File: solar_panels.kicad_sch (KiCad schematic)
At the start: 72 parts, among them U15 MAX40200AUK, U4 BQ25570RGRR, U5 BQ25570RGRR, U6 MAX40200AUK

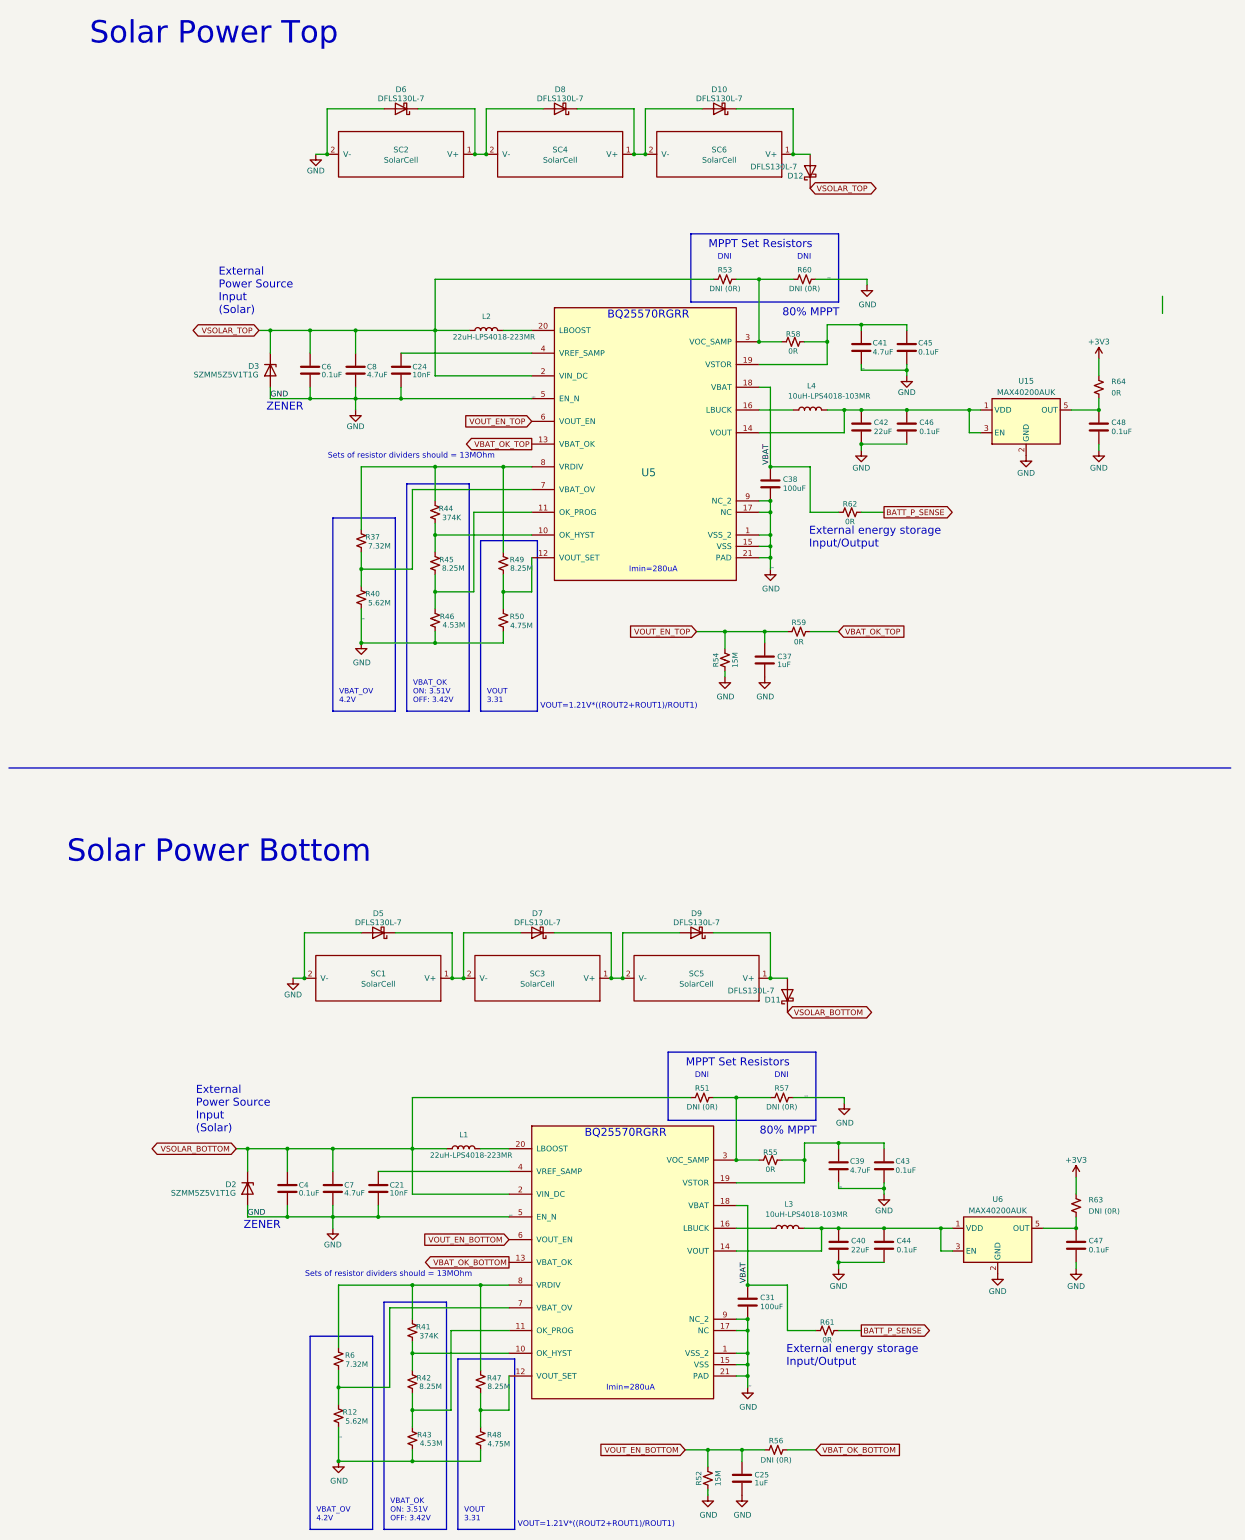
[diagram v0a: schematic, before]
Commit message: Fix ERC warnings
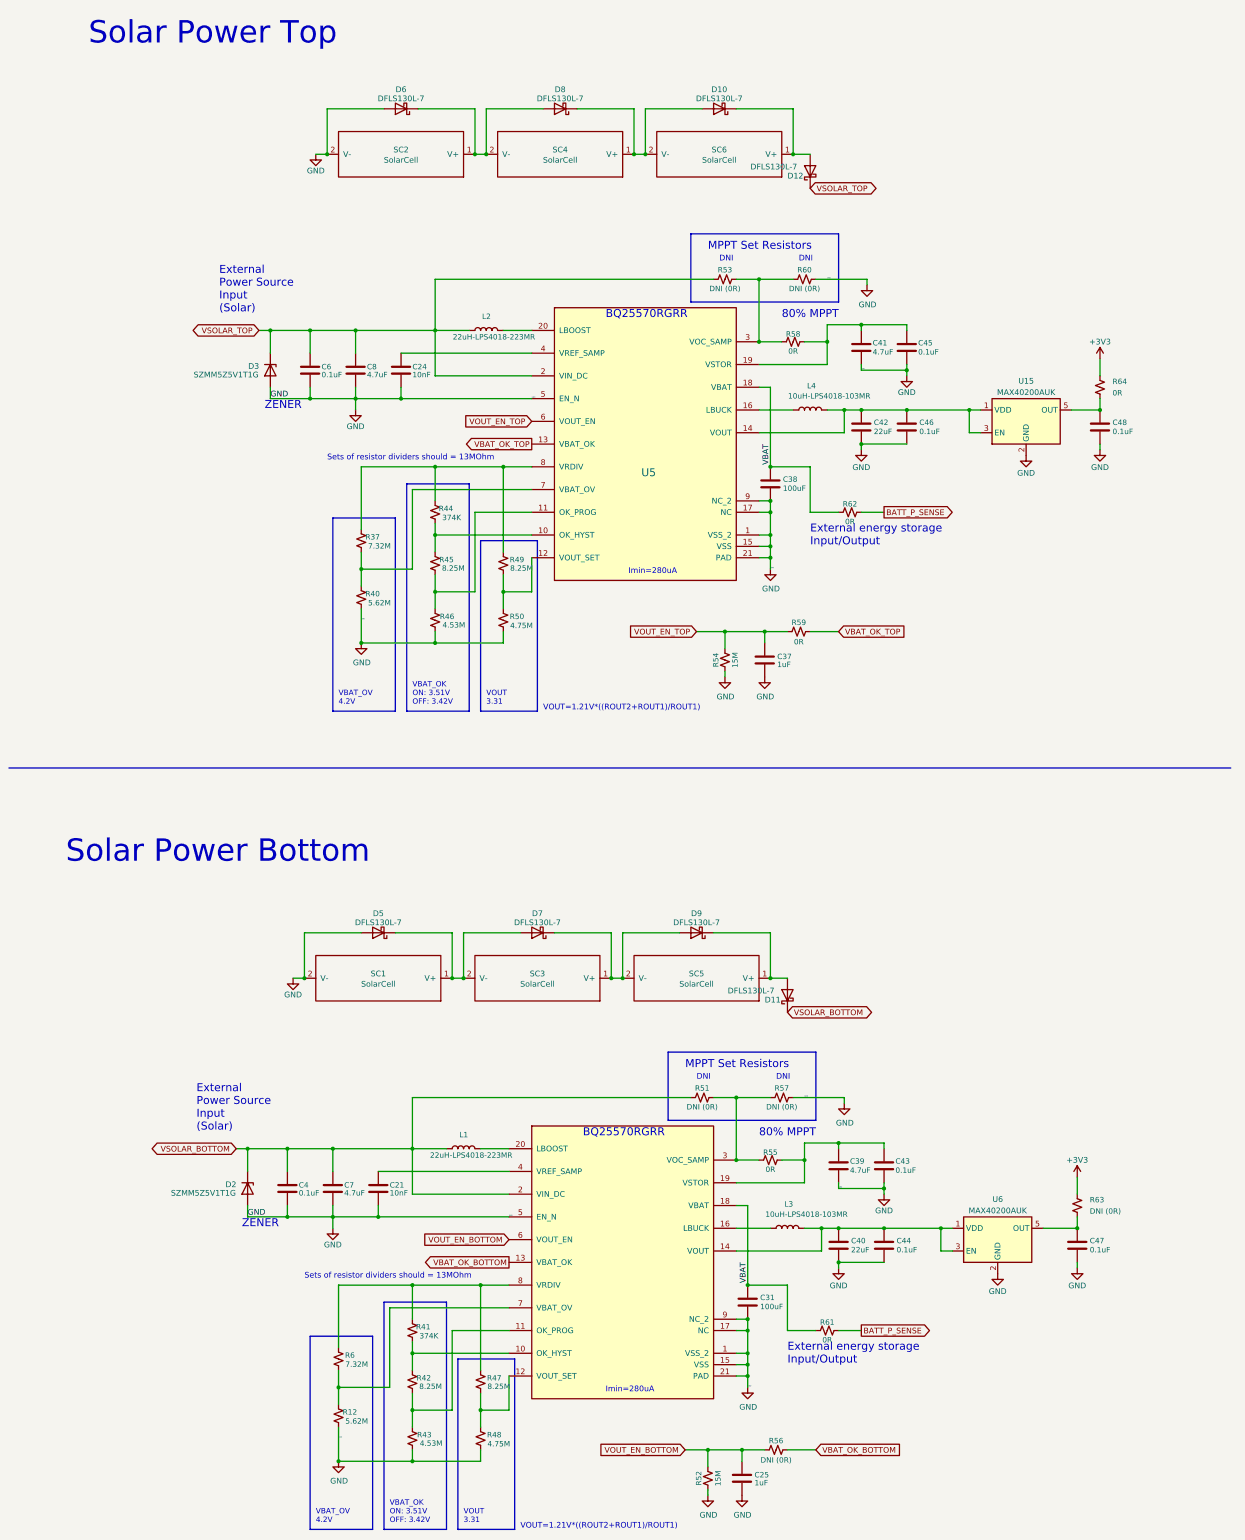
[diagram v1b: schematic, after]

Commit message: Reannotate schematic
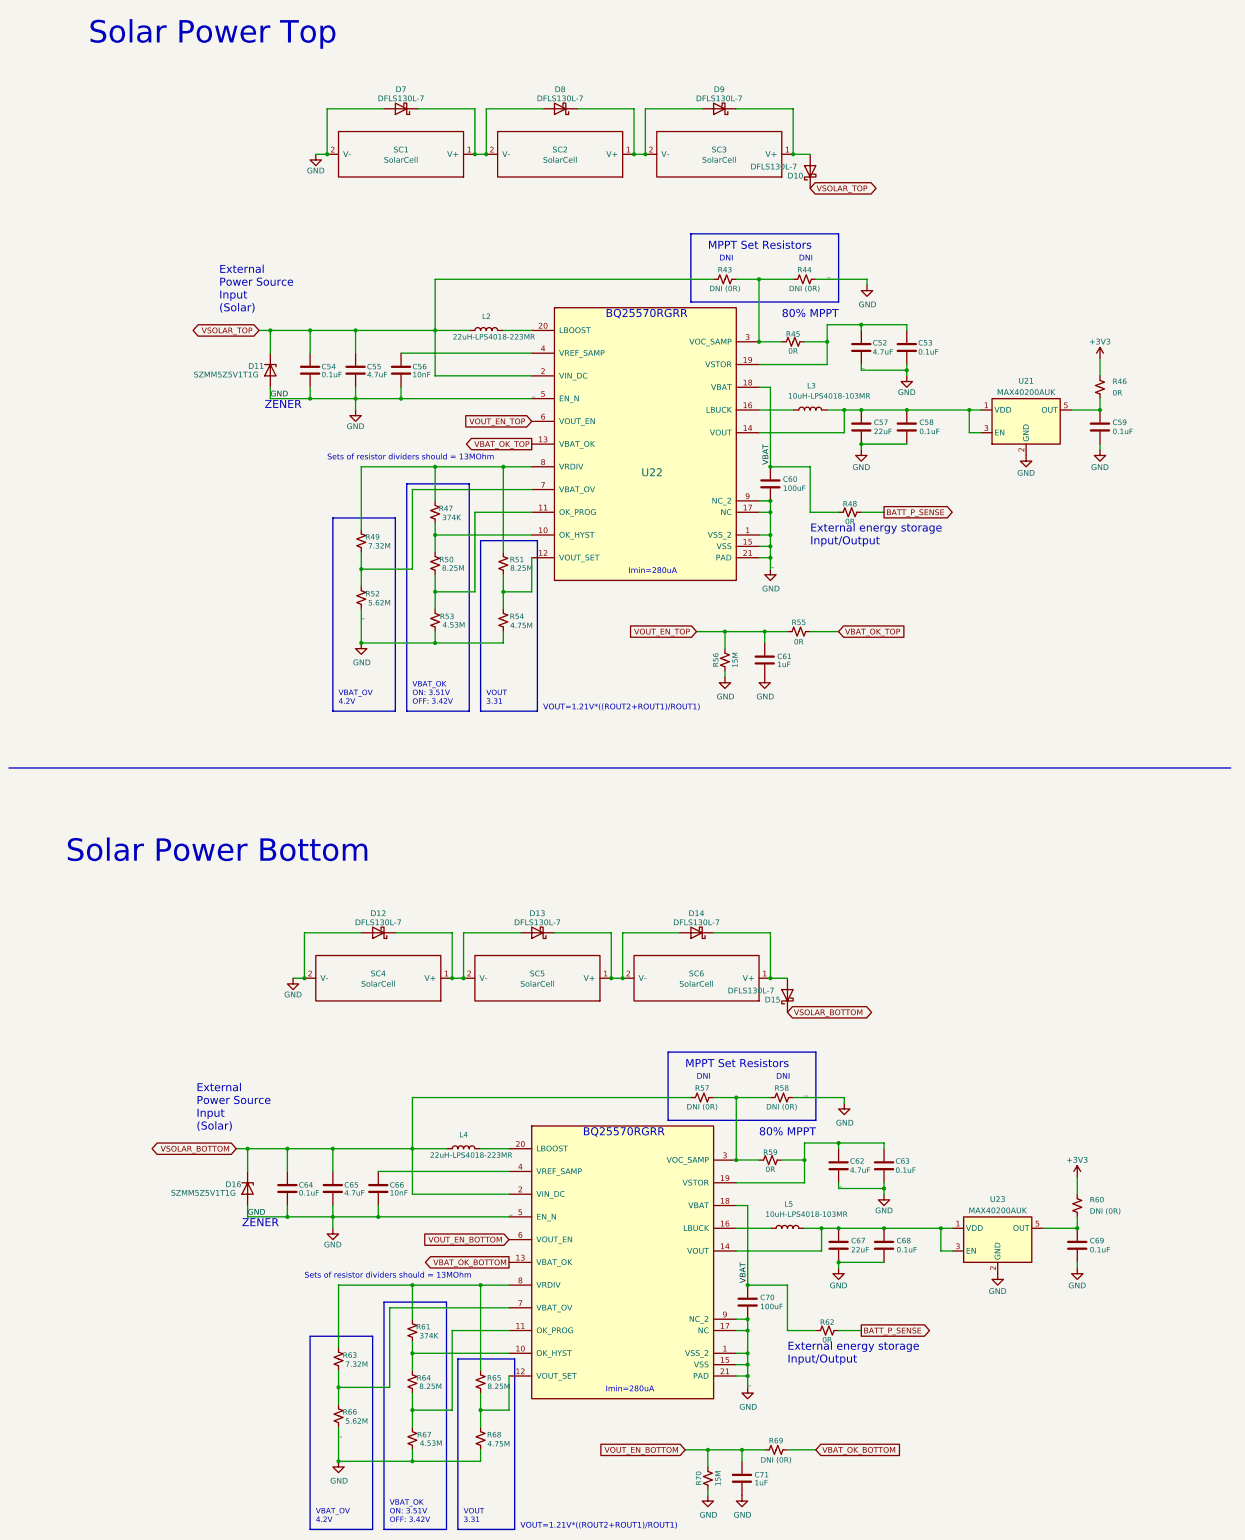
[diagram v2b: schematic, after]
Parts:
- renumbered C41 to C52, C45 to C53, C6 to C54, C8 to C55, C24 to C56, C42 to C57, C46 to C58, C48 to C59, C38 to C60, C37 to C61, C39 to C62, C43 to C63, C4 to C64, C7 to C65, C21 to C66, C40 to C67, C44 to C68, C47 to C69, C31 to C70, C25 to C71, D12 to D10, D3 to D11, D5 to D12, D7 to D13, D9 to D14, D11 to D15, D2 to D16, D6 to D7, D10 to D9, L4 to L3, L1 to L4, L3 to L5, R53 to R43, R60 to R44, R58 to R45, R64 to R46, R44 to R47, R62 to R48, R37 to R49, R45 to R50, R49 to R51, R40 to R52, R46 to R53, R50 to R54, R59 to R55, R54 to R56, R51 to R57, R57 to R58, R55 to R59, R63 to R60, R41 to R61, R61 to R62, R6 to R63, R42 to R64, R47 to R65, R12 to R66, R43 to R67, R48 to R68, R56 to R69, R52 to R70, SC2 to SC1, SC4 to SC2, SC6 to SC3, SC1 to SC4, SC3 to SC5, SC5 to SC6, U15 to U21, U5 to U22, U6 to U23, U4 to U24

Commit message: Fix inconsistencies in symbol fields
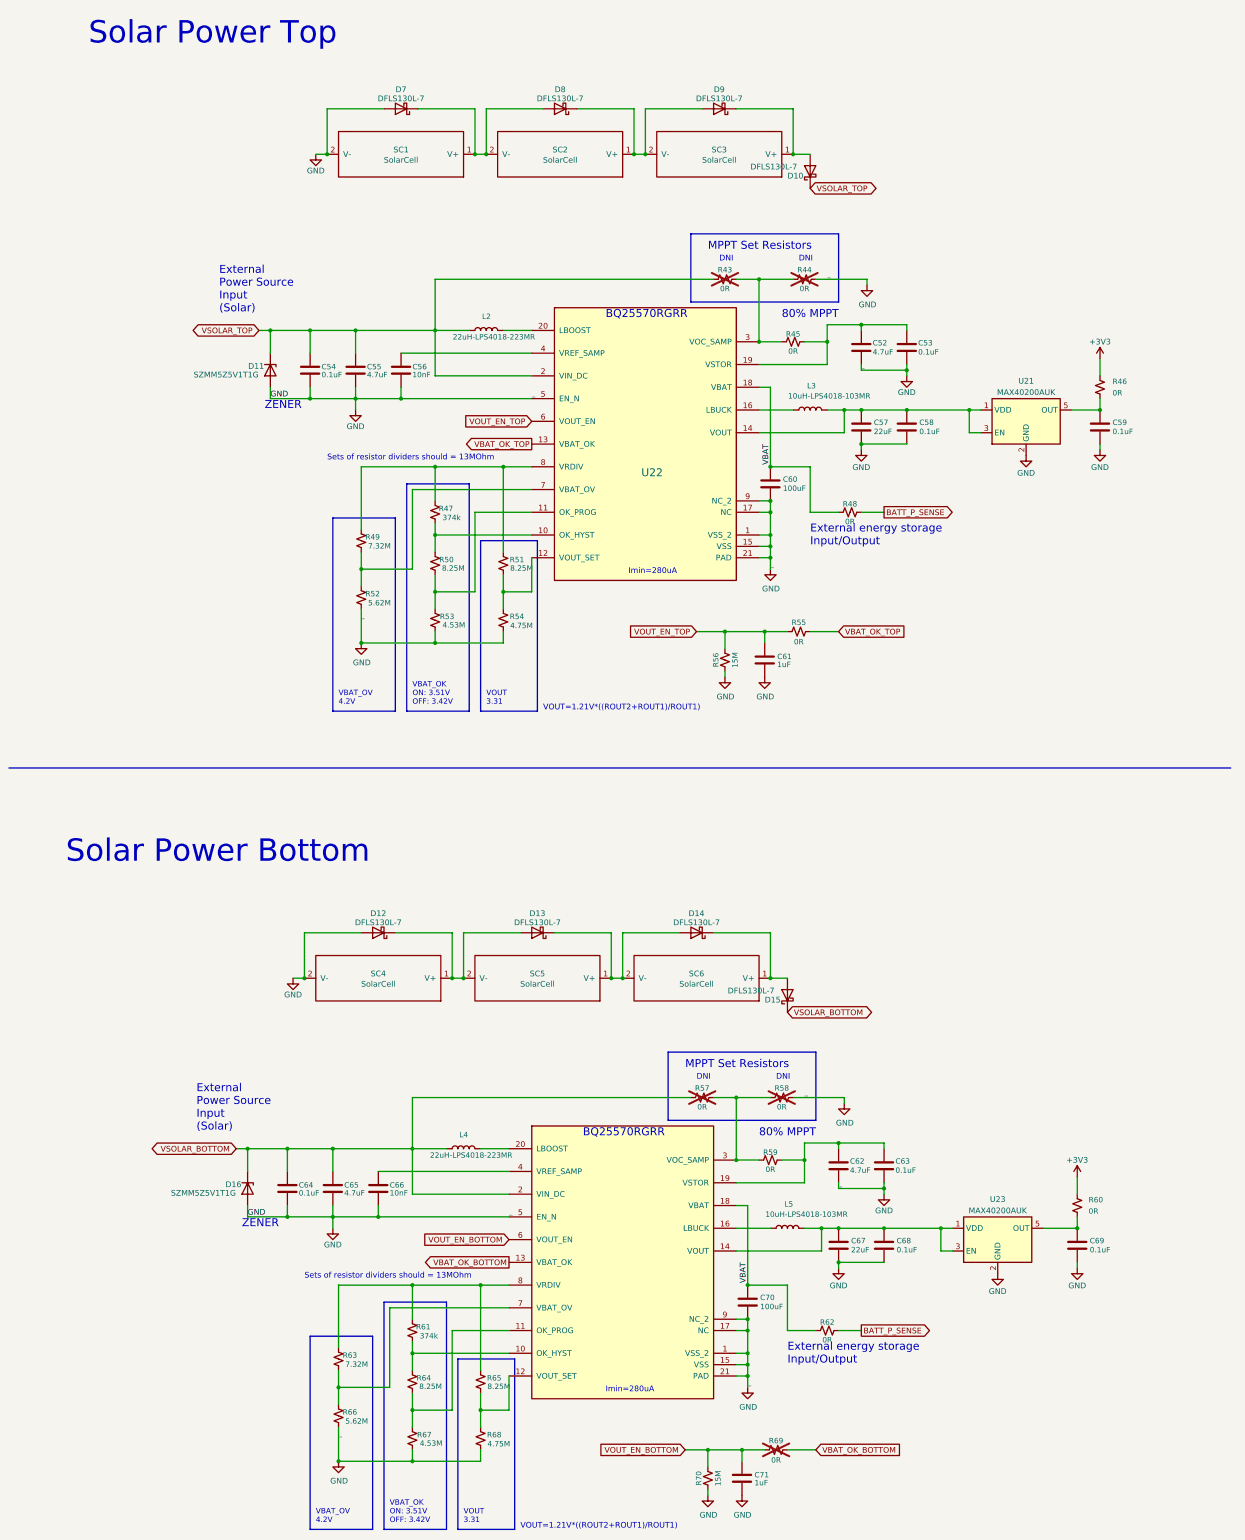
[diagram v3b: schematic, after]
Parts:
- R43, R44, R57, R58, R69: value DNI (0R) -> 0R; now not fitted
- R47, R61: value 374K -> 374k
- R60: value DNI (0R) -> 0R
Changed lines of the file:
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@@
 			)
 		)
-		(property "Value" "374K"
+		(property "Value" "374k"
 			(at 105.283 318.135 0)
 			(effects
@@
 		(in_bom yes)
 		(on_board yes)
-		(dnp no)
+		(dnp yes)
 		(property "Reference" "R43"
 			(at 171.45 79.883 90)
@@
 			)
 		)
-		(property "Value" "DNI (0R)"
+		(property "Value" "0R"
 			(at 171.45 82.677 90)
 			(effects
@@
 		(in_bom yes)
 		(on_board yes)
-		(dnp no)
+		(dnp yes)
 		(property "Reference" "R44"
 			(at 189.23 79.883 90)
@@
 			)
 		)
-		(property "Value" "DNI (0R)"
+		(property "Value" "0R"
 			(at 189.23 82.677 90)
 			(effects
@@
 		(in_bom yes)
 		(on_board yes)
-		(dnp no)
+		(dnp yes)
 		(property "Reference" "R58"
 			(at 184.15 262.763 90)
@@
 			)
 		)
-		(property "Value" "DNI (0R)"
+		(property "Value" "0R"
 			(at 184.15 265.557 90)
 			(effects
@@
 			)
 		)
-		(property "Value" "374K"
+		(property "Value" "374k"
 			(at 110.363 135.255 0)
 			(effects
@@
 		(in_bom yes)
 		(on_board yes)
-		(dnp no)
+		(dnp yes)
 		(property "Reference" "R69"
 			(at 182.88 340.868 90)
@@
 			)
 		)
-		(property "Value" "DNI (0R)"
+		(property "Value" "0R"
 			(at 182.88 345.186 90)
 			(effects
@@
 		(fields_autoplaced yes)
 		(property "Reference" "R60"
-			(at 252.984 287.0199 0)
+			(at 252.73 287.0199 0)
 			(effects
 				(font
@@
 			)
 		)
-		(property "Value" "DNI (0R)"
-			(at 252.984 289.5599 0)
+		(property "Value" "0R"
+			(at 252.73 289.5599 0)
 			(effects
 				(font
@@
 		(in_bom yes)
 		(on_board yes)
-		(dnp no)
+		(dnp yes)
 		(property "Reference" "R57"
 			(at 166.37 262.763 90)
@@
 			)
 		)
-		(property "Value" "DNI (0R)"
+		(property "Value" "0R"
 			(at 166.37 265.557 90)
 			(effects

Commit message: Add MPNs
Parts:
- C52, C55, C62, C65: Manufacturer_Part_Number (none) -> GRT188R61E475KE13D
- C53, C54, C58, C59, C63, C64, C68, C69: Manufacturer_Part_Number (none) -> GCM188L81H104KA57D
- C56, C66: Manufacturer_Part_Number (none) -> GCM188R72A103KA37D
- C57, C67: Manufacturer_Part_Number (none) -> GRT188C80J226ME13D
- C60, C70: Manufacturer_Part_Number (none) -> GRM21BR60J107ME15L
- C61, C71: Manufacturer_Part_Number (none) -> GCM188R71E105KA64D
- D10, D12, D13, D14, D15, D7, D8, D9: Manufacturer_Part_Number (none) -> DFLS130L-7
- D11, D16: Manufacturer_Part_Number (none) -> SZMM5Z5V1T1G
- L2, L4: Manufacturer_Part_Number (none) -> LPS4018-223MRC
- L3, L5: Manufacturer_Part_Number (none) -> LPS4018-103MRC
- R43, R44, R45, R46, R48, R55, R57, R58, R59, R60, R62, R69: Manufacturer_Part_Number (none) -> ERJ-3GEY0R00V
- R47, R61: Manufacturer_Part_Number (none) -> ERJ-3EKF3743V
- R49, R63: Manufacturer_Part_Number (none) -> CRCW06037M32FKEA
- R50, R51, R64, R65: Manufacturer_Part_Number (none) -> CRCW06038M25FKEA
- R52, R66: Manufacturer_Part_Number (none) -> CRCW06035M62FKEA
- R53, R67: Manufacturer_Part_Number (none) -> CRCW06034M53FKEA
- R54, R68: Manufacturer_Part_Number (none) -> CRCW06034M75FKEA
- R56, R70: Manufacturer_Part_Number (none) -> RMCF0603JT15M0
- U21, U23: Manufacturer_Part_Number (none) -> MAX40200AUK+T
- U22, U24: Manufacturer_Part_Number (none) -> BQ25570RGRR
